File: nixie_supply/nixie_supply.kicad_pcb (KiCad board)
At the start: 2 copper layers, 66 x 50.8 mm, 28 parts, among them P1 CONN_01X02, P2 CONN_01X04, Q1 FQPF4N90CT, U1 LM741, U2 4047, U3 7805, U4 LM741, U5 4518, U6 4011

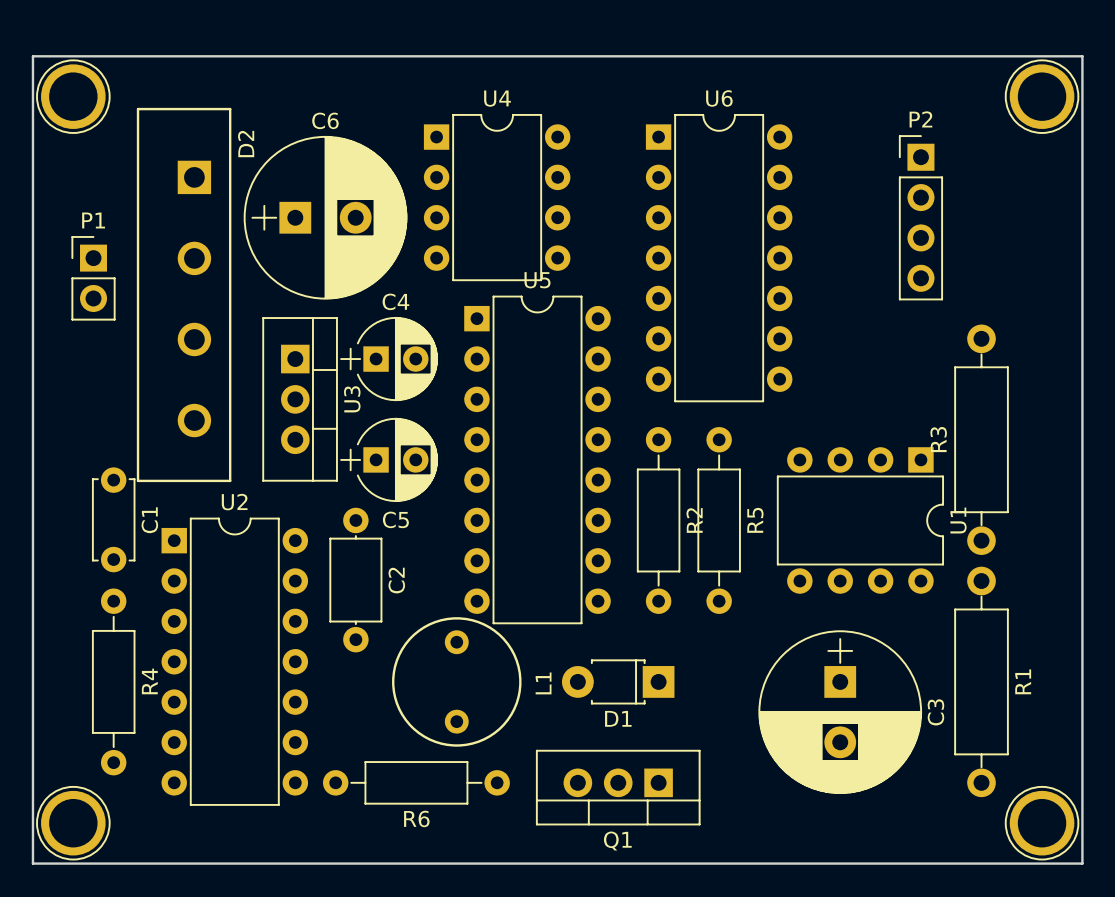
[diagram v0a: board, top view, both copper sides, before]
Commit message: Started routing for the clock
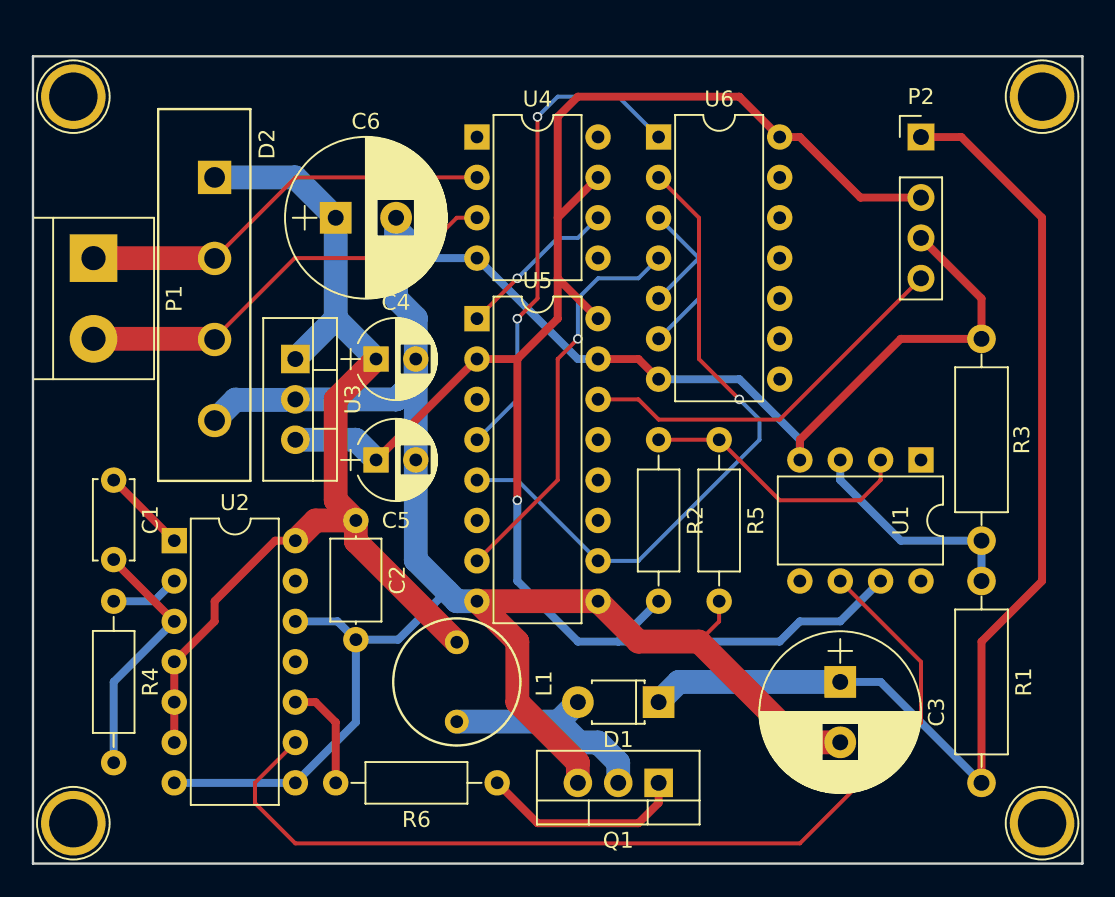
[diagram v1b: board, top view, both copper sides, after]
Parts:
- P1: footprint Pin_Headers:Pin_Header_Straight_1x02_Pitch2.54mm -> Connectors:bornier2
- P2: footprint Pin_Headers:Pin_Header_Straight_1x04_Pitch2.54mm -> hv:Pin_Header_Straight_1x04_Pitch2.54mm
- moved C6 2.54 mm to (100.3, 94.0)
- moved U4 2.54 mm to (109.2, 88.9)
- moved D1 1.27 mm to (120.7, 124.5)
- moved D2 1.27 mm to (92.7, 91.4)
- turned P1 to 270 degrees
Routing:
- net GND: track 0.00 -> 174.0 mm
- net +5V: track 0.00 -> 110.2 mm, vias 0 -> 1
- net +220V: track 0.00 -> 70.3 mm
- net +12V: track 0.00 -> 65.2 mm
- net Net-(U1-Pad6): track 0.00 -> 62.0 mm
- net Net-(U5-Pad10): track 0.00 -> 42.2 mm, vias 0 -> 1
- net Net-(U5-Pad4): track 0.00 -> 31.1 mm, vias 0 -> 2
- net +12VA: track 0.00 -> 27.3 mm
- net -12VA: track 0.00 -> 26.2 mm
- net Net-(U5-Pad7): track 0.00 -> 25.3 mm, vias 0 -> 1
- net /PPS/CLK_OUT: track 0.00 -> 24.5 mm
- net Net-(R2-Pad1): track 0.00 -> 17.3 mm
- net Net-(C1-Pad2): track 0.00 -> 15.9 mm
- net Net-(R1-Pad1): track 0.00 -> 14.3 mm
- net Net-(D1-Pad2): track 0.00 -> 14.2 mm
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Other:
- net class current_carrying added: clearance 0.4, trace_width 1.5, via_dia 0.6, via_drill 0.4
- net class high_voltage added: clearance 1, trace_width 0.5, via_dia 0.6, via_drill 0.4

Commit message: Supply board mk2: reduced time base noise, upped some clearances, added ground plane
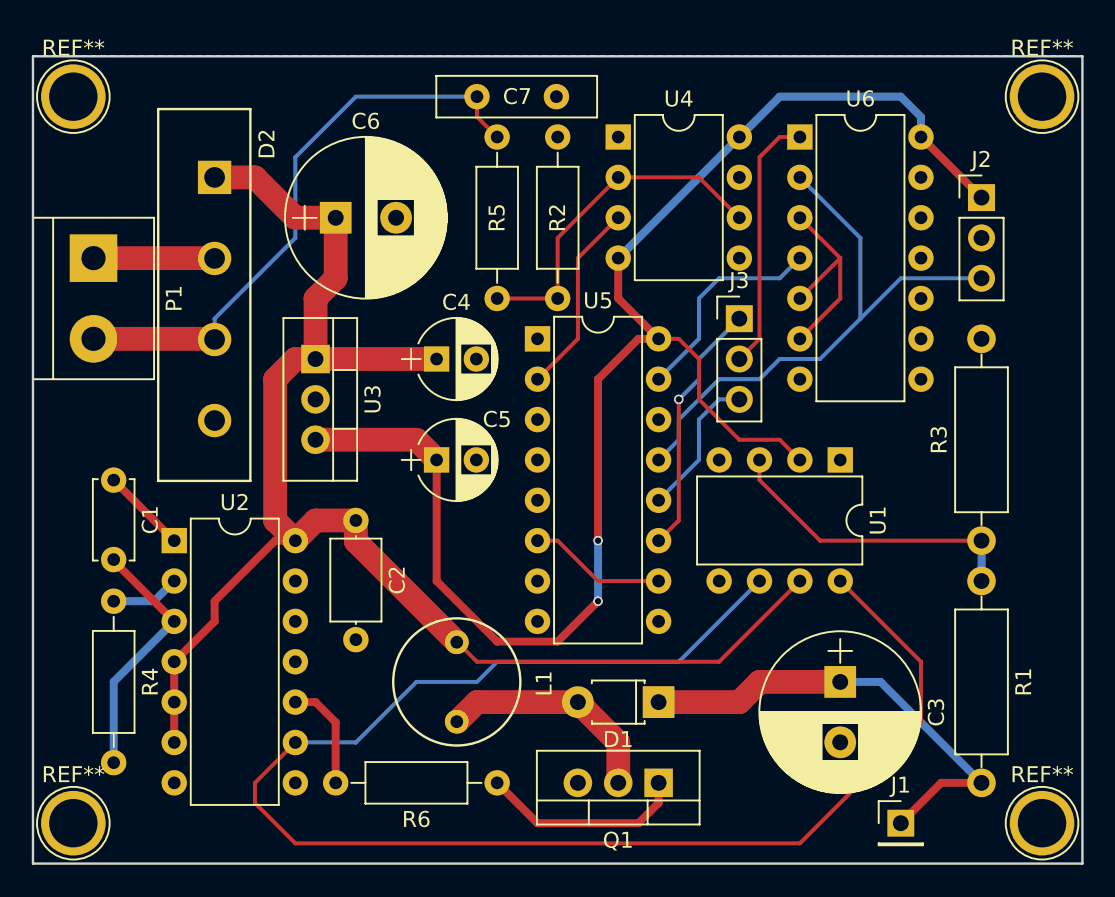
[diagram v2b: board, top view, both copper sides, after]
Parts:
- removed P2: CONN_01X04, hv:Pin_Header_Straight_1x04_Pitch2.54mm
- added C7: 220pf (221), Capacitors_THT:C_Disc_D10.0mm_W2.5mm_P5.00mm, F.Cu at (109.2, 86.4)
- added J1: CONN_01X01, Pin_Headers:Pin_Header_Straight_1x01_Pitch2.54mm, F.Cu at (135.9, 132.1)
- added J2: CONN_01X03, Pin_Headers:Pin_Header_Straight_1x03_Pitch2.54mm, F.Cu at (141.0, 92.7)
- added J3: CONN_01X03, Pin_Headers:Pin_Header_Straight_1x03_Pitch2.54mm, F.Cu at (125.7, 100.3)
- R2: value 1.2K -> 33k
- R5: value 4.7K -> 10K
- U4: value LM741 -> LM555N
- moved R2 21.6 mm to (110.5, 88.9)
- moved R5 13.5 mm to (114.3, 99.1), turned to 90 degrees
- moved U4 8.89 mm to (118.1, 88.9)
- moved U6 8.89 mm to (129.5, 88.9)
- moved U1 5.08 mm to (132.1, 109.2)
- moved U5 4.02 mm to (113.0, 101.6)
- moved C4 3.81 mm to (106.7, 102.9)
- moved C5 3.81 mm to (106.7, 109.2)
- moved U3 1.27 mm to (99.1, 102.9)
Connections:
- R2 pad 1: Net-(R2-Pad1) -> +12VA
- R2 pad 2: +5V -> Net-(R2-Pad2)
- R5 pad 1: Net-(R2-Pad1) -> Net-(R2-Pad2)
- U1 pad 2: Net-(R2-Pad1) -> +5V
- U1 pad 7: +5V -> +12V
- U4 pad 1: Net-(U4-Pad1) -> GND
- U4 pad 2: -12VA -> Net-(R2-Pad2)
- U4 pad 3: +12VA -> Net-(U4-Pad3)
- U4 pad 4: GND -> +5V
- U4 pad 6: Net-(U4-Pad6) -> Net-(R2-Pad2)
- U4 pad 7: +5V -> Net-(U4-Pad7)
- U4 pad 8: (no net) -> +5V
- U5 pad 1: Net-(U4-Pad6) -> GND
- U5 pad 13: Net-(U5-Pad13) -> /PPS/CLK_OUT
- U5 pad 14: /PPS/CLK_OUT -> Net-(U5-Pad14)
- U5 pad 15: GND -> Net-(U5-Pad15)
- U5 pad 2: +5V -> Net-(U4-Pad3)
- U5 pad 5: Net-(U5-Pad10) -> Net-(U5-Pad5)
- U5 pad 6: Net-(U5-Pad6) -> Net-(U5-Pad10)
- U5 pad 7: Net-(U5-Pad7) -> GND
- U6 pad 1: Net-(U5-Pad4) -> Net-(J3-Pad2)
- U6 pad 2: Net-(U5-Pad10) -> /PPS/CLK_OUT
- U6 pad 4: Net-(U5-Pad7) -> Net-(U5-Pad15)
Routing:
- net GND: track 174.0 -> 0.02 mm
- net +220V: track 70.3 -> 29.6 mm
- net Net-(U5-Pad10): track 42.2 -> 8.67 mm, vias 1 -> 0
- net Net-(U1-Pad6): track 62.0 -> 95.4 mm
- net Net-(U5-Pad4): track 31.1 -> 0.00 mm, vias 2 -> 0
- net +12V: track 65.2 -> 94.9 mm
- net Net-(U5-Pad7): track 25.3 -> 0.00 mm, vias 1 -> 0
- net Net-(R2-Pad2): track 0.00 -> 21.7 mm
- net -12VA: track 26.2 -> 7.64 mm
- net Net-(R2-Pad1): track 17.3 -> 0.00 mm
- net Net-(J3-Pad2): track 0.00 -> 16.3 mm
- net Net-(J3-Pad1): track 0.00 -> 16.1 mm, vias 0 -> 1
- net Net-(U5-Pad15): track 0.00 -> 13.5 mm
- net +5V: track 110.2 -> 97.5 mm, vias 1 -> 2
- net Net-(U4-Pad3): track 0.00 -> 12.3 mm
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- added copper zone on B.Cu, net GND
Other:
- net class current_carrying: clearance 0.4 -> 0.2

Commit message: Added more noise reduction to clock signal, added top ground plane
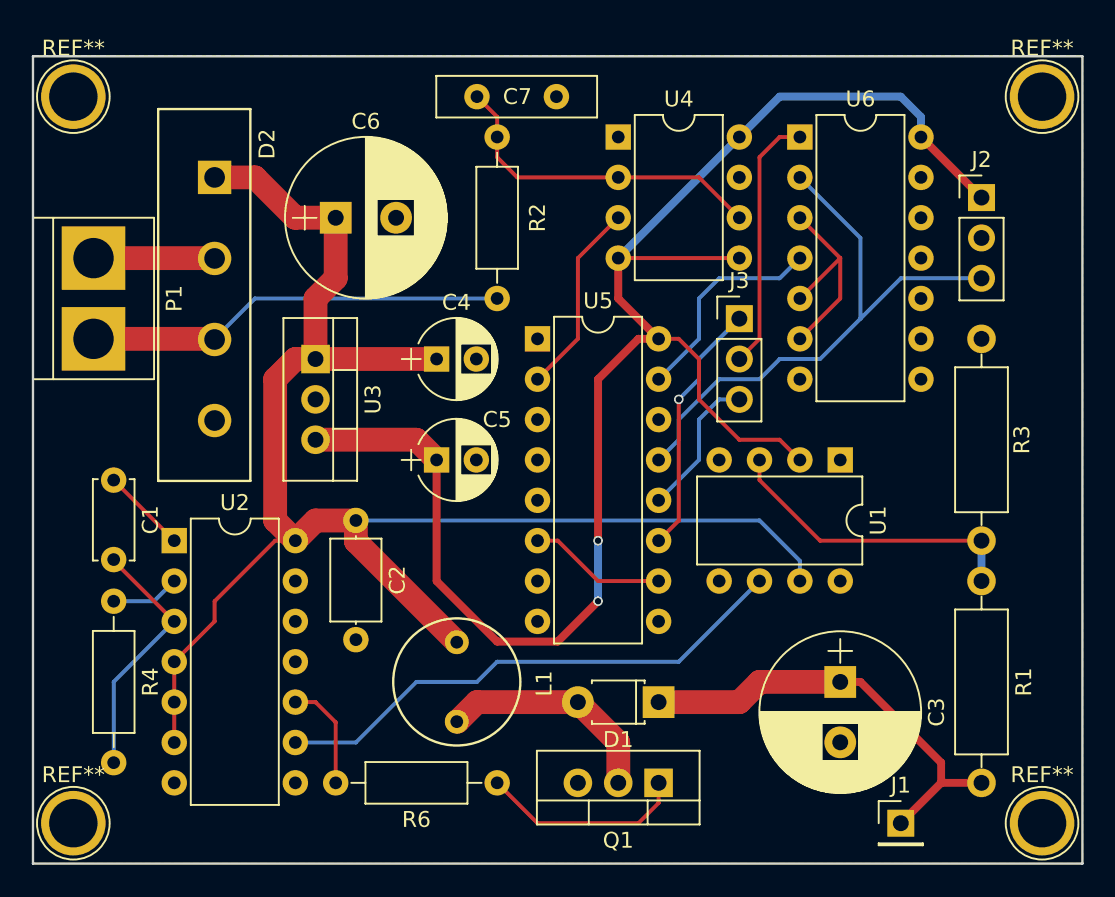
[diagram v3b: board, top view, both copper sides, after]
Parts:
- removed R5: 10K, Resistors_THT:R_Axial_DIN0207_L6.3mm_D2.5mm_P10.16mm_Horizontal
- C7: value 220pf (221) -> 0.1uF
- R2: value 33k -> 1K
- moved R2 10.2 mm to (110.5, 99.1), turned to 90 degrees
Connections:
- net +220V renamed +240V
- C7 pad 1: +12VA -> Net-(C7-Pad1)
- R2 pad 2: Net-(R2-Pad2) -> Net-(C7-Pad1)
- U4 pad 2: Net-(R2-Pad2) -> Net-(C7-Pad1)
- U4 pad 5: Net-(U4-Pad5) -> +5V
- U4 pad 6: Net-(R2-Pad2) -> Net-(C7-Pad1)
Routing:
- net Net-(U1-Pad6): track 95.4 -> 33.4 mm
- net Net-(R2-Pad2): track 21.7 -> 0.00 mm
- net Net-(C7-Pad1): track 0.00 -> 21.2 mm
- net +12VA: track 37.3 -> 26.5 mm
- net +5V: track 97.5 -> 105.1 mm
- net +12V: track 94.9 -> 101.0 mm
- net +240V: track 29.6 -> 27.8 mm
- added copper zone on F.Cu, net GND

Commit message: Added more isolation on the HV transient netclass
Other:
- net class transient added: clearance 0.5, trace_width 1.5, via_dia 0.6, via_drill 0.4
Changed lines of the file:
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@@
     (add_net "Net-(C1-Pad2)")
     (add_net "Net-(C7-Pad1)")
-    (add_net "Net-(D1-Pad2)")
     (add_net "Net-(J3-Pad1)")
     (add_net "Net-(J3-Pad2)")
@@
     (uvia_drill 0.1)
     (add_net +240V)
+  )
+  (net_class transient ""
+    (clearance 0.5)
+    (trace_width 1.5)
+    (via_dia 0.6)
+    (via_drill 0.4)
+    (uvia_dia 0.3)
+    (uvia_drill 0.1)
+    (add_net "Net-(D1-Pad2)")
   )
   (module Housings_DIP:DIP-14_W7.62mm (layer F.Cu)
@@
   (segment (start 86.36 115.49) (end 86.36 115.57) (width 0.5) (layer F.Cu) (net 2))
   (segment (start 86.36 115.57) (end 90.17 119.38) (width 0.25) (layer F.Cu) (net 2))
-  (segment (start 129.54 116.84) (end 129.54 115.57) (width 0.25) (layer B.Cu) (net 3) (status 400000))
-  (segment (start 127 113.03) (end 101.6 113.03) (width 0.25) (layer B.Cu) (net 3) (status 800000))
+  (segment (start 129.54 116.84) (end 129.54 115.57) (width 0.25) (layer B.Cu) (net 3))
+  (segment (start 127 113.03) (end 101.6 113.03) (width 0.25) (layer B.Cu) (net 3))
   (segment (start 129.54 115.57) (end 127 113.03) (width 0.25) (layer B.Cu) (net 3))
   (segment (start 99.06 102.87) (end 97.79 102.87) (width 1.5) (layer F.Cu) (net 3))
@@
   (segment (start 128.27 97.79) (end 124.46 97.79) (width 0.25) (layer B.Cu) (net 30))
   (segment (start 138.43 129.54) (end 138.43 128.27) (width 0.5) (layer F.Cu) (net 31))
-  (segment (start 133.35 123.19) (end 132.08 123.19) (width 0.5) (layer F.Cu) (net 31) (status 800000))
+  (segment (start 133.35 123.19) (end 132.08 123.19) (width 0.5) (layer F.Cu) (net 31))
   (segment (start 138.43 128.27) (end 133.35 123.19) (width 0.5) (layer F.Cu) (net 31))
   (segment (start 140.97 129.54) (end 138.43 129.54) (width 0.5) (layer F.Cu) (net 31))
@@
   (segment (start 125.73 93.98) (end 123.19 91.44) (width 0.25) (layer F.Cu) (net 32))
   (segment (start 123.19 91.44) (end 118.11 91.44) (width 0.25) (layer F.Cu) (net 32))
-  (zone (net 4) (net_name GND) (layer F.Cu) (hatch edge 0.508)
+  (zone (net 4) (net_name GND) (layer B.Cu) (hatch edge 0.508)
     (connect_pads (clearance 0.5))
     (min_thickness 0.254)
@@
     )
   )
-  (zone (net 4) (net_name GND) (layer B.Cu) (hatch edge 0.508)
+  (zone (net 4) (net_name GND) (layer F.Cu) (hatch edge 0.508)
     (connect_pads (clearance 0.5))
     (min_thickness 0.254)
